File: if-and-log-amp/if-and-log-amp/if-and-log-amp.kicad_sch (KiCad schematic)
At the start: 65 parts, among them J301 Conn_Coaxial, J306 Conn_Coaxial, SW301 Video, U301 AD603AQ, U302 L78L05_TO92, U303 LM317L_TO92, U304 AD8307AN, U305 CA3140

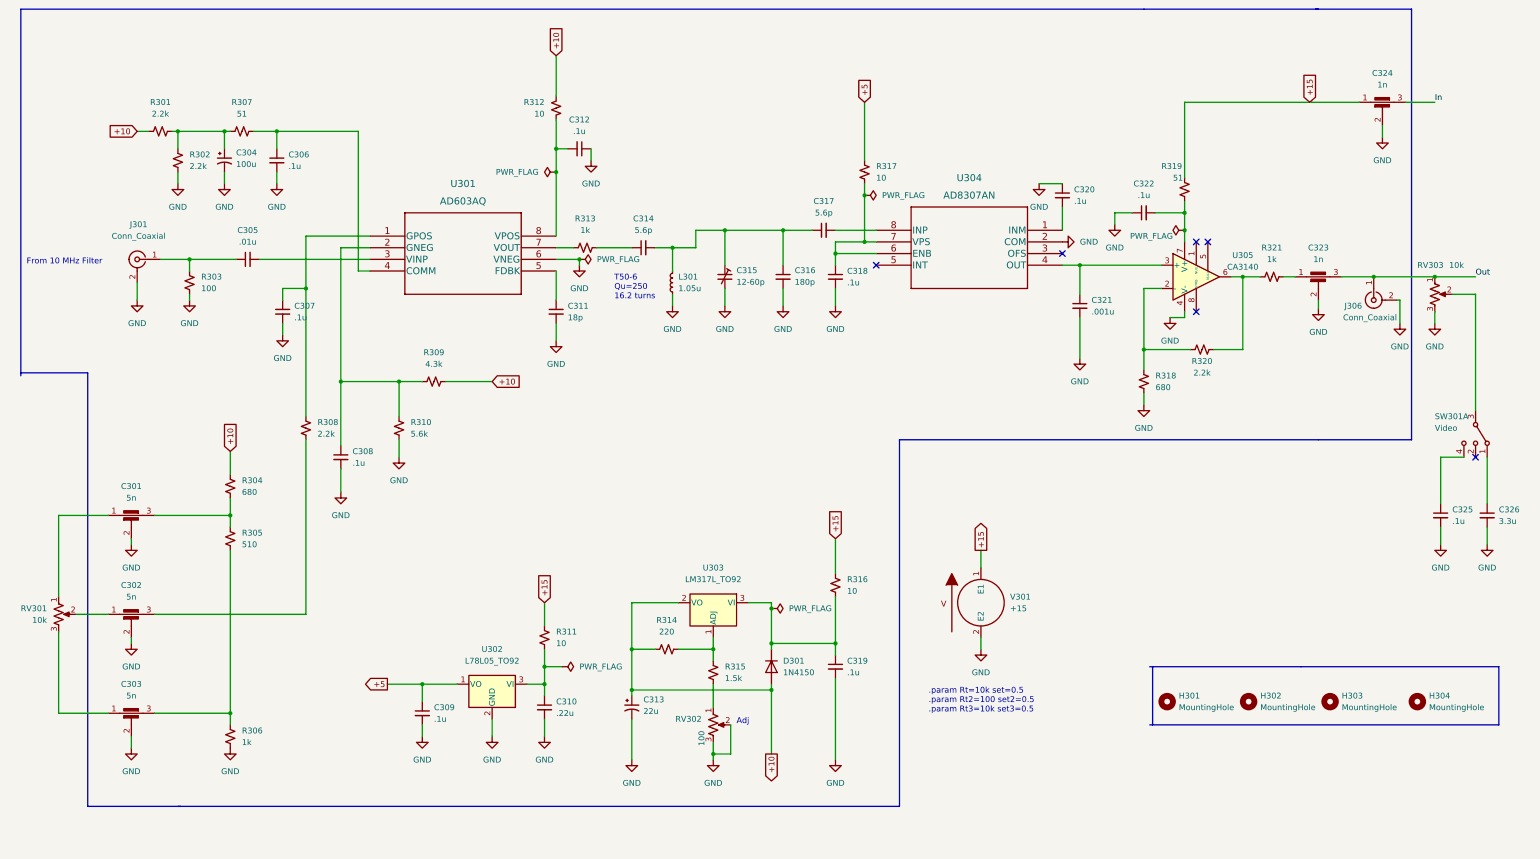
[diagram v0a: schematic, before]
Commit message: revised if and log amp schematic and board
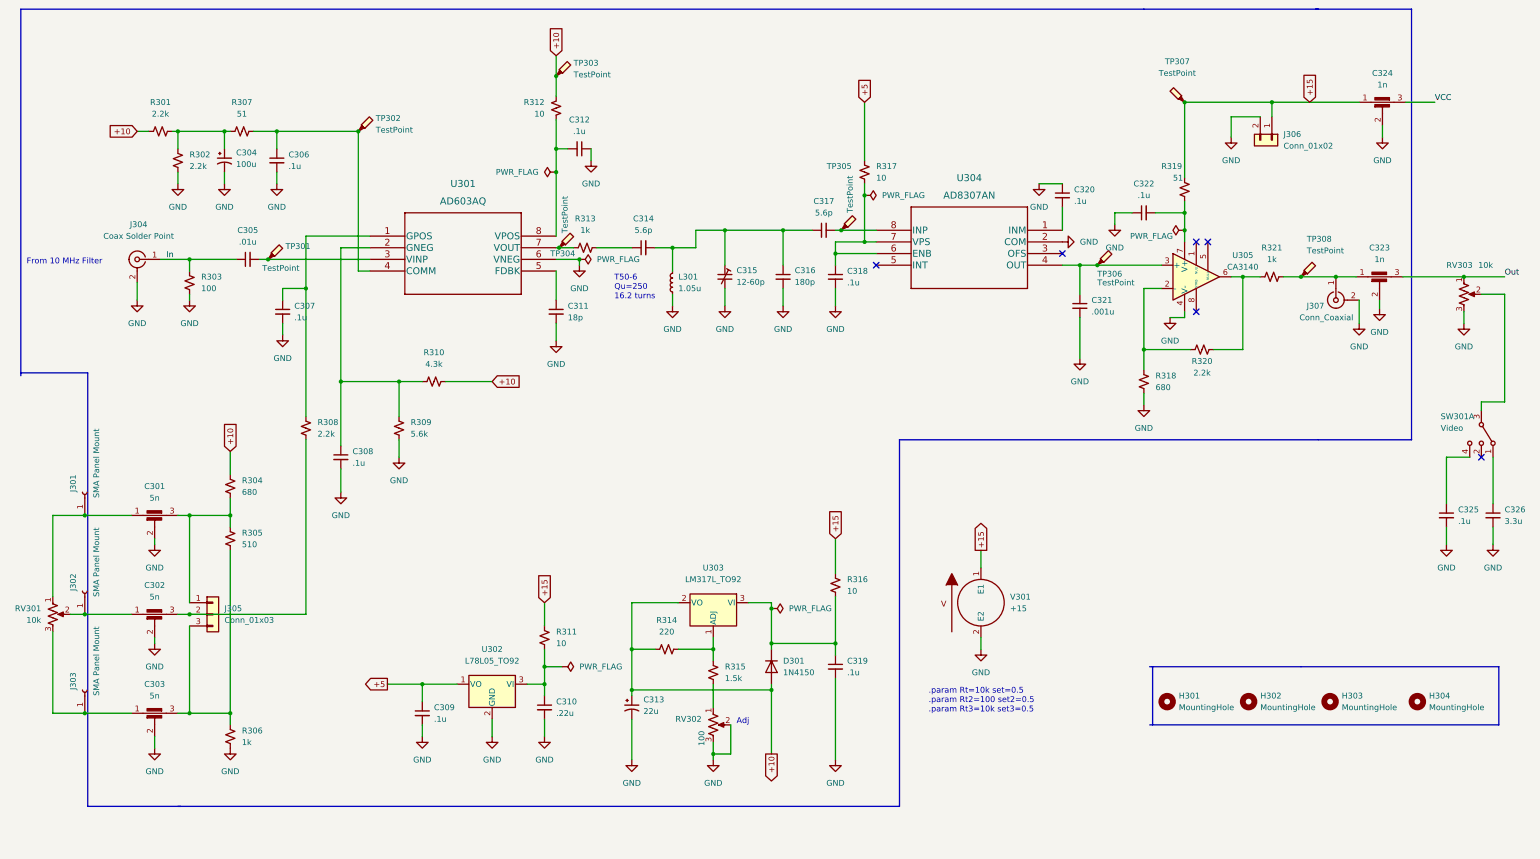
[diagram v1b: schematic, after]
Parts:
- added J301, J302, J303: SMA Panel Mount, symbol Connector:Conn_01x01_Female
- added J305: Conn_01x03, Connector_Wire:SolderWire-0.5sqmm_1x03_P4.6mm_D0.9mm_OD2.1mm, symbol Connector_Generic:Conn_01x03
- added J306: Conn_01x02, if-log-amp:691103110002, symbol Connector_Generic:Conn_01x02
- added TP301, TP302, TP303, TP304, TP305, TP306, TP307, TP308: TestPoint, TestPoint:TestPoint_Pad_1.0x1.0mm, symbol Connector:TestPoint_Probe
- C305, C306, C307, C308, C309, C310, C311, C312, C314, C316, C317, C318, C319, C320, C322: footprint Capacitor_THT:CP_Radial_D5.0mm_P2.50mm -> Capacitor_THT:C_Disc_D5.0mm_W2.5mm_P5.00mm
- J304: renamed from J301; value Conn_Coaxial -> Coax Solder Point; footprint if-log-amp:MOLEX_73391-0060 -> Connector_Wire:SolderWire-0.5sqmm_1x02_P4.6mm_D0.9mm_OD2.1mm
- J307: renamed from J306; footprint if-log-amp:MOLEX_73391-0060 -> Connector_Wire:SolderWire-0.5sqmm_1x02_P4.6mm_D0.9mm_OD2.1mm
- renumbered R310 to R309, R309 to R310
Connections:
- net +10: now also TP303.1
- net +15: now also J306.1 (Pin_1), TP307.1
- net GND: now also J306.2 (Pin_2)
- net In: now also C305.1, J304.1 (In), R303.1; no longer C324.3
- net Out: no longer J307.1 (In)
- net at C321.1, U304.4 (OUT), U305.3 (+): now also TP306.1
- net at C302.1, RV301.2: now also J302.1 (Pin_1)
- net at C302.3, R308.2: now also J305.2 (Pin_2)
- net at C301.3, R304.2, R305.1: now also J305.1 (Pin_1)
- net at C303.3, R305.2, R306.1: now also J305.3 (Pin_3)
- net at C301.1, RV301.1: now also J301.1 (Pin_1)
- net at C303.1, RV301.3: now also J303.1 (Pin_1)
- net at C323.1, R321.2: now also J307.1 (In), TP308.1
- net at C317.2, U304.8 (INP): now also TP305.1
- net at C306.1, R307.2, U301.4 (COMM): now also TP302.1
- net at R313.1, U301.7 (VOUT): now also TP304.1
- net at C305.2, U301.3 (VINP): now also TP301.1
- new net VCC: C324.3
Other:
- moved on the sheet: C301, C302, C303, C323, C325, C326, J307, RV301, RV303, SW301A

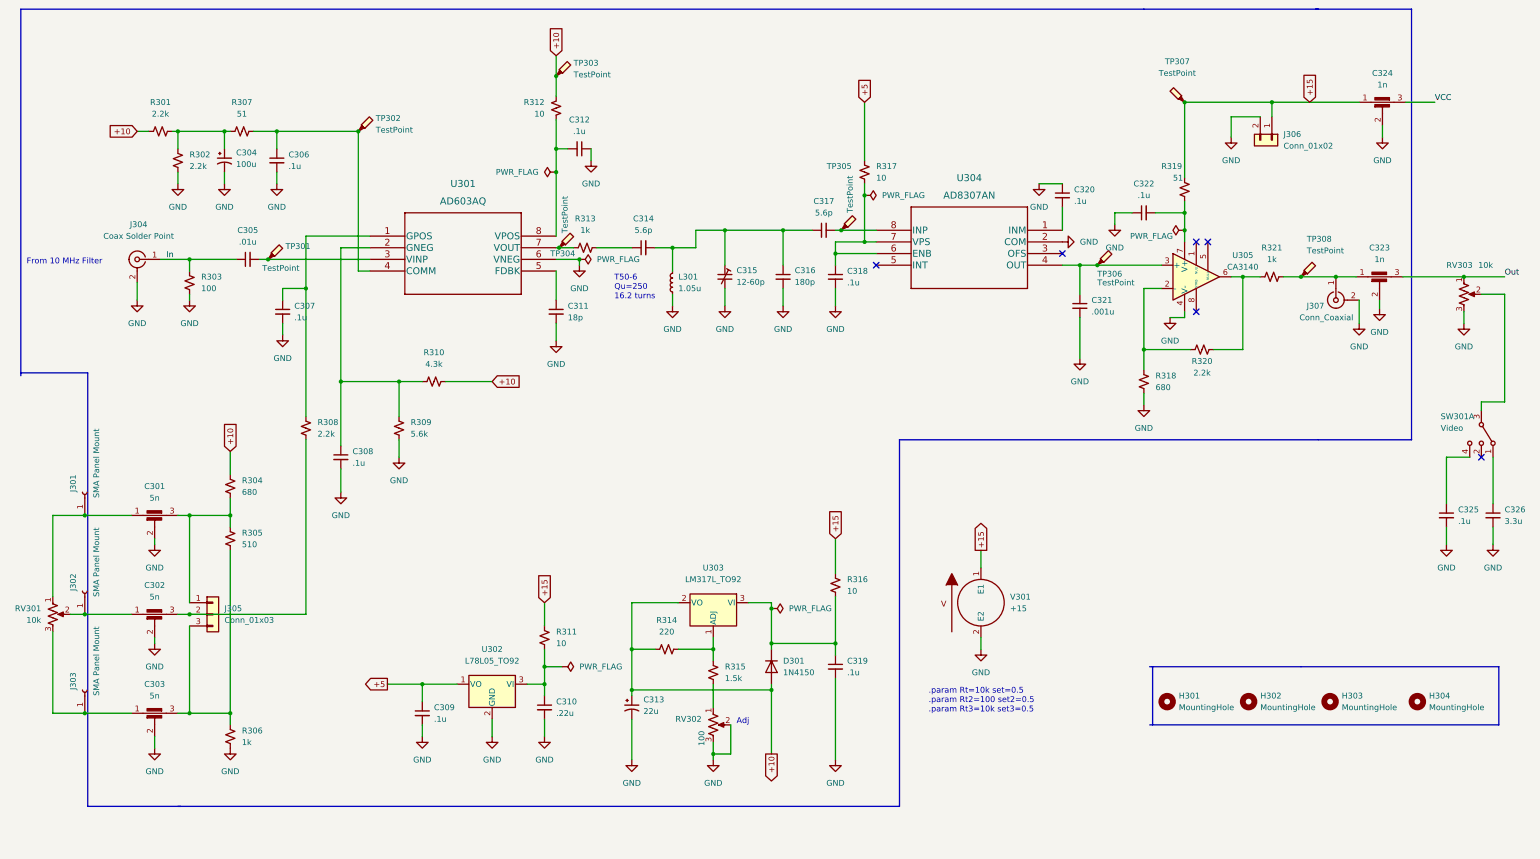
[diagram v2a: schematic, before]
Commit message: Add amp to if-and-log-amp
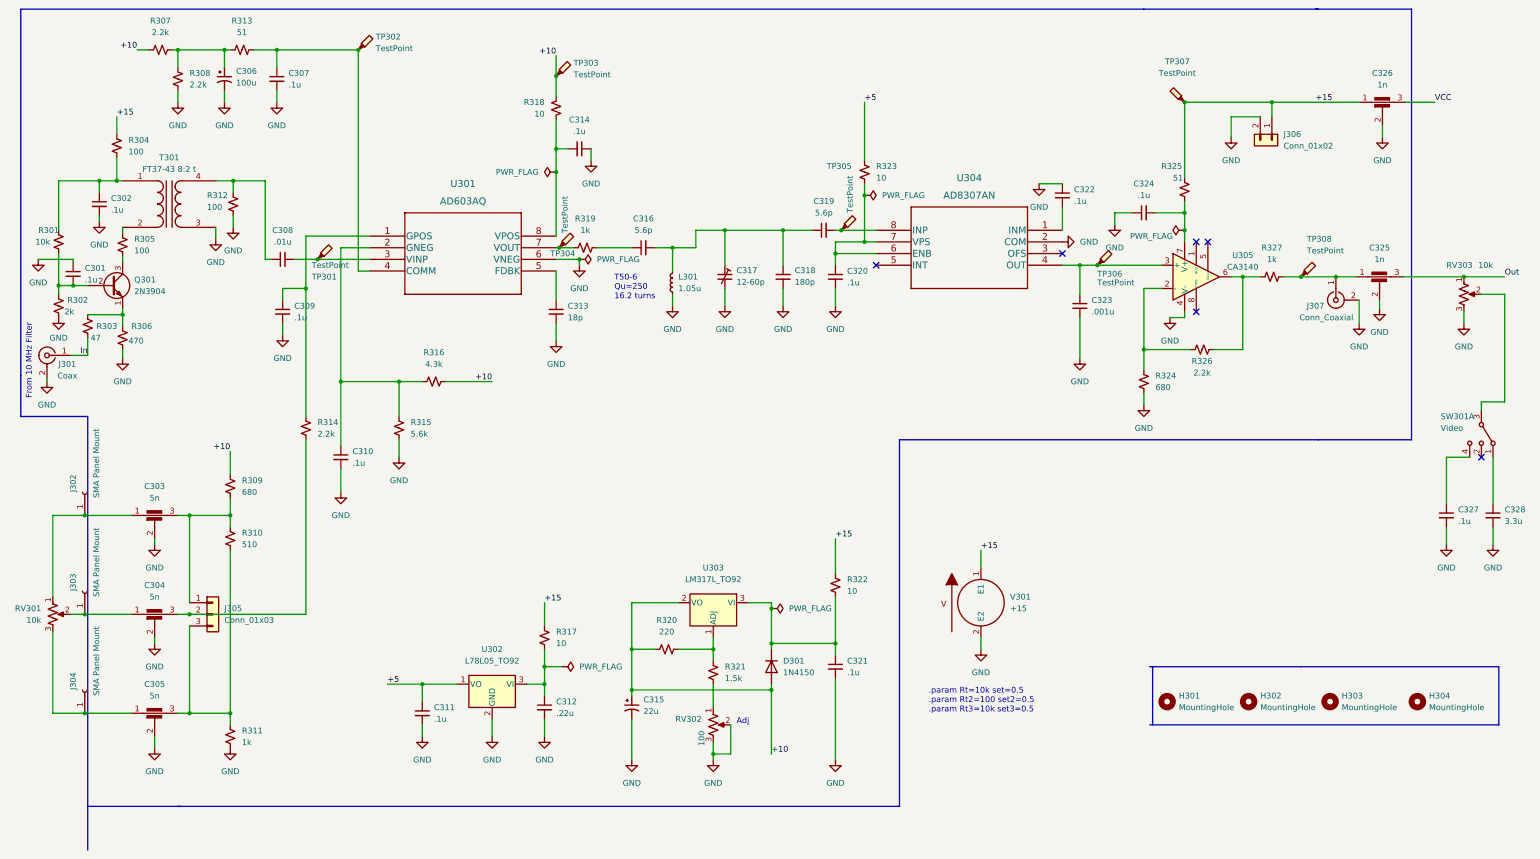
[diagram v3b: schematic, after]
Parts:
- added C301, C302: .1u, Capacitor_THT:C_Disc_D5.0mm_W2.5mm_P5.00mm, symbol Device:C_Small
- added Q301: 2N3904, Package_TO_SOT_THT:TO-92_Inline, symbol Transistor_BJT:2N3904
- added R301: 10k, Resistor_THT:R_Axial_DIN0207_L6.3mm_D2.5mm_P7.62mm_Horizontal, symbol Device:R_Small_US
- added R302: 2k, Resistor_THT:R_Axial_DIN0207_L6.3mm_D2.5mm_P7.62mm_Horizontal, symbol Device:R_Small_US
- added R303: 47, Resistor_THT:R_Axial_DIN0207_L6.3mm_D2.5mm_P7.62mm_Horizontal, symbol Device:R_Small_US
- added R304, R305: 100, Resistor_THT:R_Axial_DIN0207_L6.3mm_D2.5mm_P7.62mm_Horizontal, symbol Device:R_Small_US
- added R306: 470, Resistor_THT:R_Axial_DIN0207_L6.3mm_D2.5mm_P7.62mm_Horizontal, symbol Device:R_Small_US
- added T301: FT37-43 8:2 t, Transformer_THT:Transformer_Toroid_Horizontal_D14.0mm_Amidon-T50, symbol Device:Transformer_1P_1S
- J301: renamed from J304; value Coax Solder Point -> Coax
- renumbered C301 to C303, C302 to C304, C303 to C305, C304 to C306, C306 to C307, C305 to C308, C307 to C309, C308 to C310, C309 to C311, C310 to C312, C311 to C313, C312 to C314, C313 to C315, C314 to C316, C315 to C317, C316 to C318, C317 to C319, C318 to C320, C319 to C321, C320 to C322, C321 to C323, C322 to C324, C323 to C325, C324 to C326, C325 to C327, C326 to C328, J301 to J302, J302 to J303, J303 to J304, R301 to R307, R302 to R308, R304 to R309, R305 to R310, R306 to R311, R303 to R312, R307 to R313, R308 to R314, R309 to R315, R310 to R316, R311 to R317, R312 to R318, R313 to R319, R314 to R320, R315 to R321, R316 to R322, R317 to R323, R318 to R324, R319 to R325, R320 to R326, R321 to R327
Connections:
- net +15: now also R304.1
- net GND: now also C301.1, C302.2, R302.2, R306.2, T301.3 (SA)
- net In: now also R303.2; no longer C308.1, R312.1
- new net: Q301.1 (E), R303.1, R306.1
- new net: C302.1, R301.1, R304.2, T301.1 (AA)
- new net: R305.1, T301.2 (AB)
- new net: C308.1, R312.1, T301.4 (SB)
- new net: C301.2, Q301.2 (B), R301.2, R302.1
- new net: Q301.3 (C), R305.2
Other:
- moved on the sheet: C306, C307, C308, J301, R307, R308, R312, R313, TP301, TP302

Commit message: 2db-div schematic added
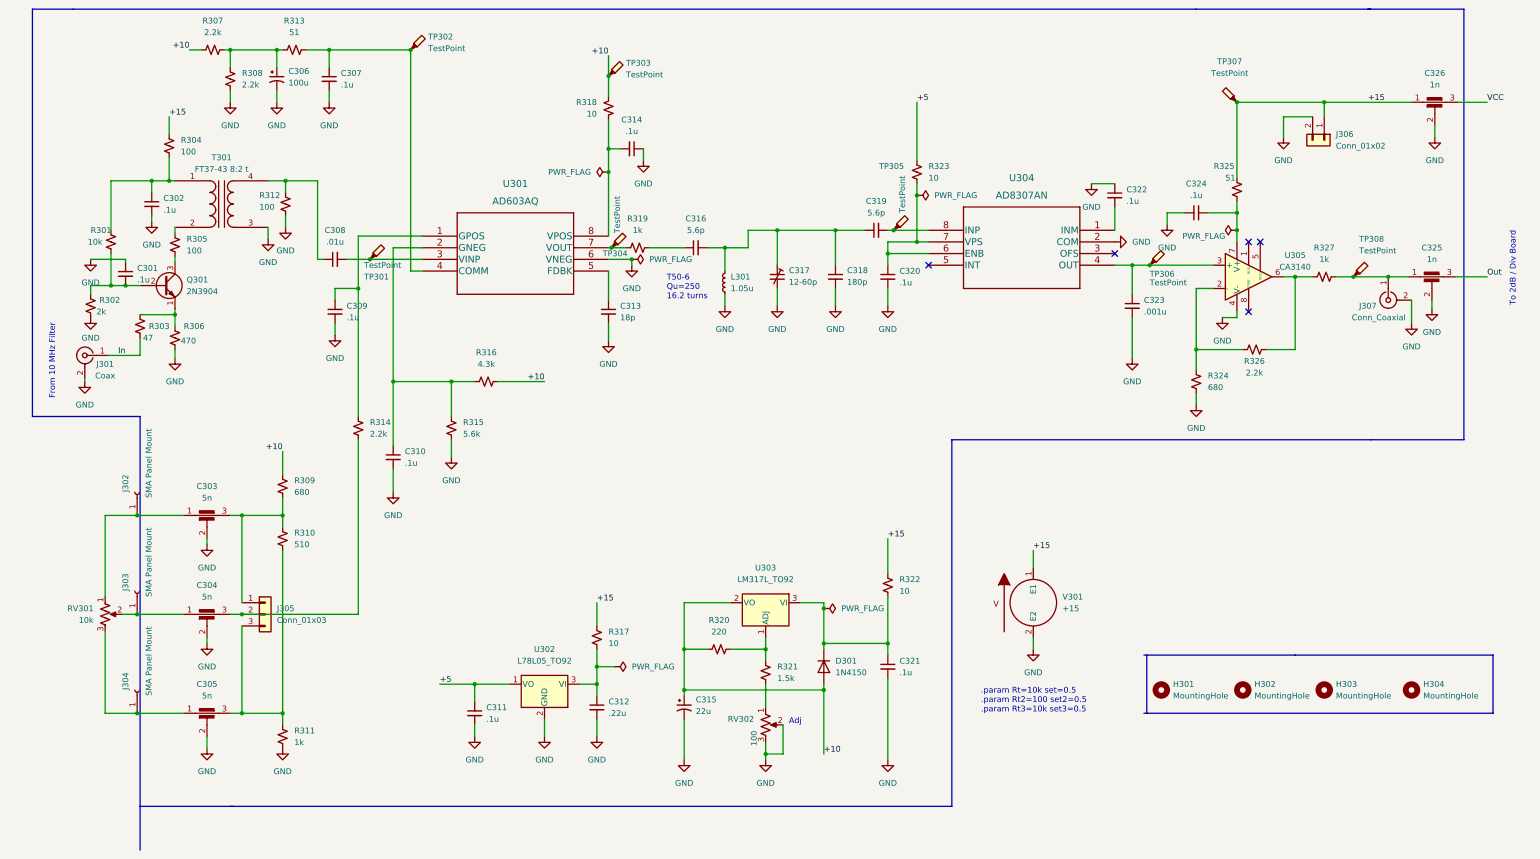
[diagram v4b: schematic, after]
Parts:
- removed C327: .1u, symbol Device:C_Small
- removed C328: 3.3u, symbol Device:C_Small
- removed RV303: 10k, symbol Device:R_Potentiometer_US
- removed SW301: Video, symbol Switch:SW_DP3T
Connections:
- no-connect marks 6 -> 5
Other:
- note added: "To 2dB / Div Board"
- moved on the sheet: C301, C302, C303, C304, C305, C306, C307, C308, C309, C310, C311, C312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

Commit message: improved if and log amp and second lo/mixer
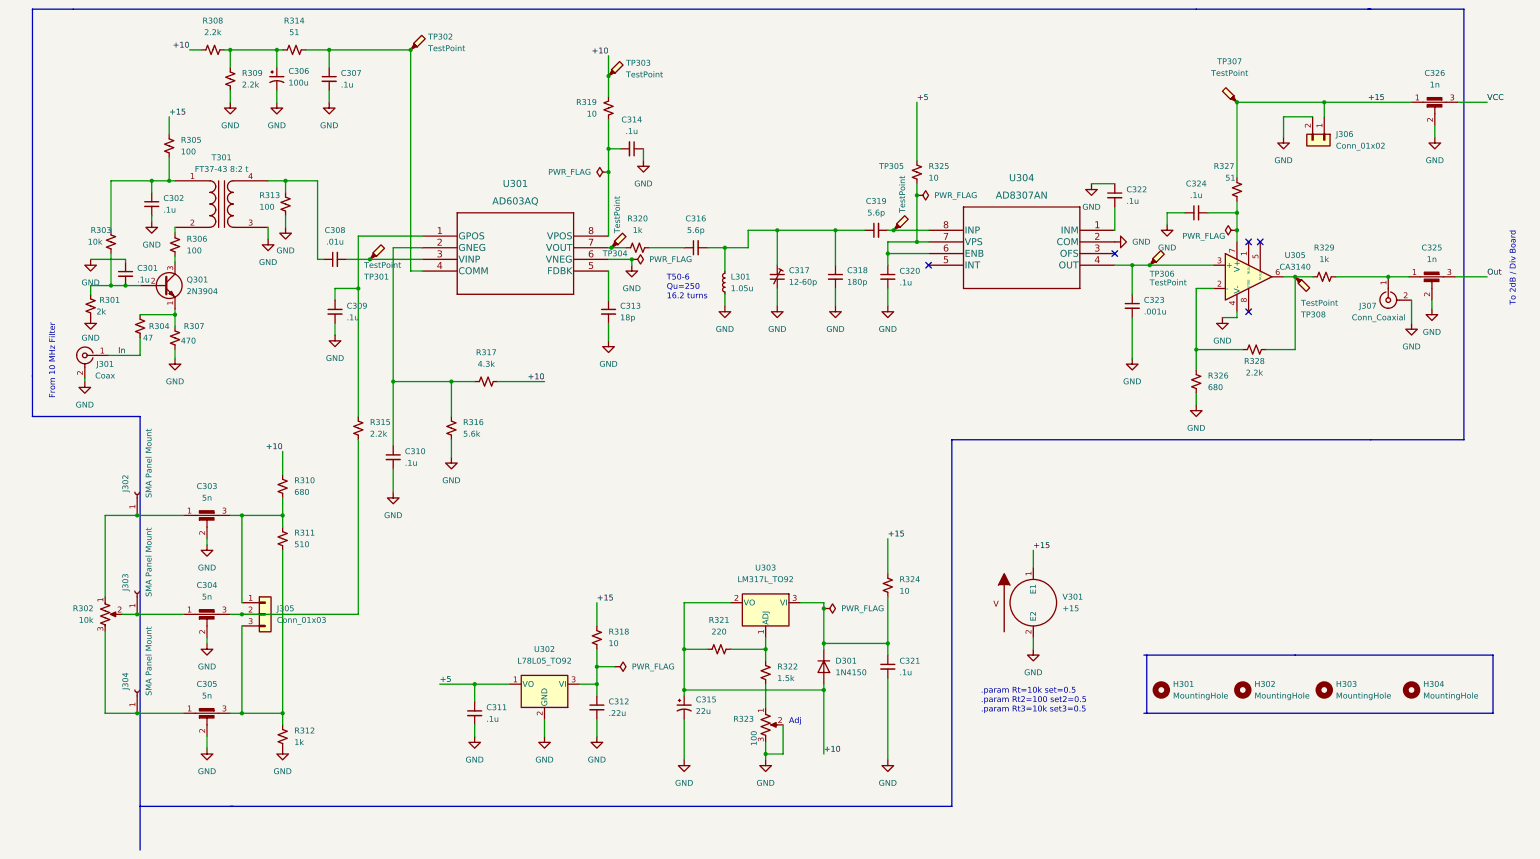
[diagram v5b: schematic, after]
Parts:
- renumbered R302 to R301, RV301 to R302, R301 to R303, R303 to R304, R304 to R305, R305 to R306, R306 to R307, R307 to R308, R308 to R309, R309 to R310, R310 to R311, R311 to R312, R312 to R313, R313 to R314, R314 to R315, R315 to R316, R316 to R317, R317 to R318, R318 to R319, R319 to R320, R320 to R321, R321 to R322, RV302 to R323, R322 to R324, R323 to R325, R324 to R326, R325 to R327, R326 to R328, R327 to R329
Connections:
- net at R328.1, R329.1, U305.6: now also TP308.1
- net at C325.1, J307.1 (In), R329.2: no longer TP308.1
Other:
- moved on the sheet: TP308

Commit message: v7 conversion
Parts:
- D301: Spice_Lib_File if-log-amp-spice\fairch.lib -> (none); Spice_Model 1N4152 -> (none); Spice_Netlist_Enabled Y -> (none); Spice_Node_Sequence 2 1 -> (none); Spice_Primitive D -> (none)
- J301, J307: Spice_Model Conn_Coaxial -> (none); Spice_Netlist_Enabled N -> (none); Spice_Primitive J -> (none)
- J302, J303, J304: Spice_Model SMA Panel Mount -> (none); Spice_Netlist_Enabled N -> (none); Spice_Primitive J -> (none)
- R302: Spice_Lib_File if-log-amp-spice\Pot.lib -> (none); Spice_Model pot_alps_a -> (none); Spice_Netlist_Enabled Y -> (none); Spice_Primitive X -> (none)
- R323: Spice_Lib_File if-log-amp-spice\Pot2.lib -> (none); Spice_Model pot_lin2 -> (none); Spice_Netlist_Enabled Y -> (none); Spice_Primitive X -> (none)
- TP301, TP302, TP303, TP304, TP305, TP306, TP307: value TestPoint -> ${SIM.PARAMS}; Spice_Netlist_Enabled N -> (none)
- TP308: value TestPoint -> ${SIM.PARAMS}; Spice_Netlist_Enabled N -> (none); Spice_Primitive R -> (none)
- U301: Spice_Lib_File if-log-amp-spice\ad603a.cir -> (none); Spice_Model AD603A -> (none); Spice_Netlist_Enabled Y -> (none); Spice_Primitive X -> (none)
- U302: Spice_Lib_File if-log-amp-spice\78L05_TEST.sub -> (none); Spice_Model X78L05 -> (none); Spice_Netlist_Enabled Y -> (none); Spice_Node_Sequence 3 2 1 -> (none); Spice_Primitive X -> (none)
- U303: Spice_Lib_File if-log-amp-spice\lm317.lib -> (none); Spice_Model LM317TI -> (none); Spice_Netlist_Enabled Y -> (none); Spice_Node_Sequence 3 1 2 -> (none); Spice_Primitive X -> (none)
- U304: value AD8307AN -> ${SIM.PARAMS}; Spice_Netlist_Enabled N -> (none); Spice_Primitive R -> (none)
- U305: Spice_Lib_File if-log-amp-spice\ca3140.sub -> (none); Spice_Model ca3140 -> (none); Spice_Netlist_Enabled Y -> (none); Spice_Primitive X -> (none)
- V301: value +15 -> 15; Spice_Model dc 15 -> (none); Spice_Netlist_Enabled Y -> (none); Spice_Primitive V -> (none)
